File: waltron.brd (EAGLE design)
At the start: 45.4 x 47 mm, 21 parts, among them IC1 4049N, U1 LM386

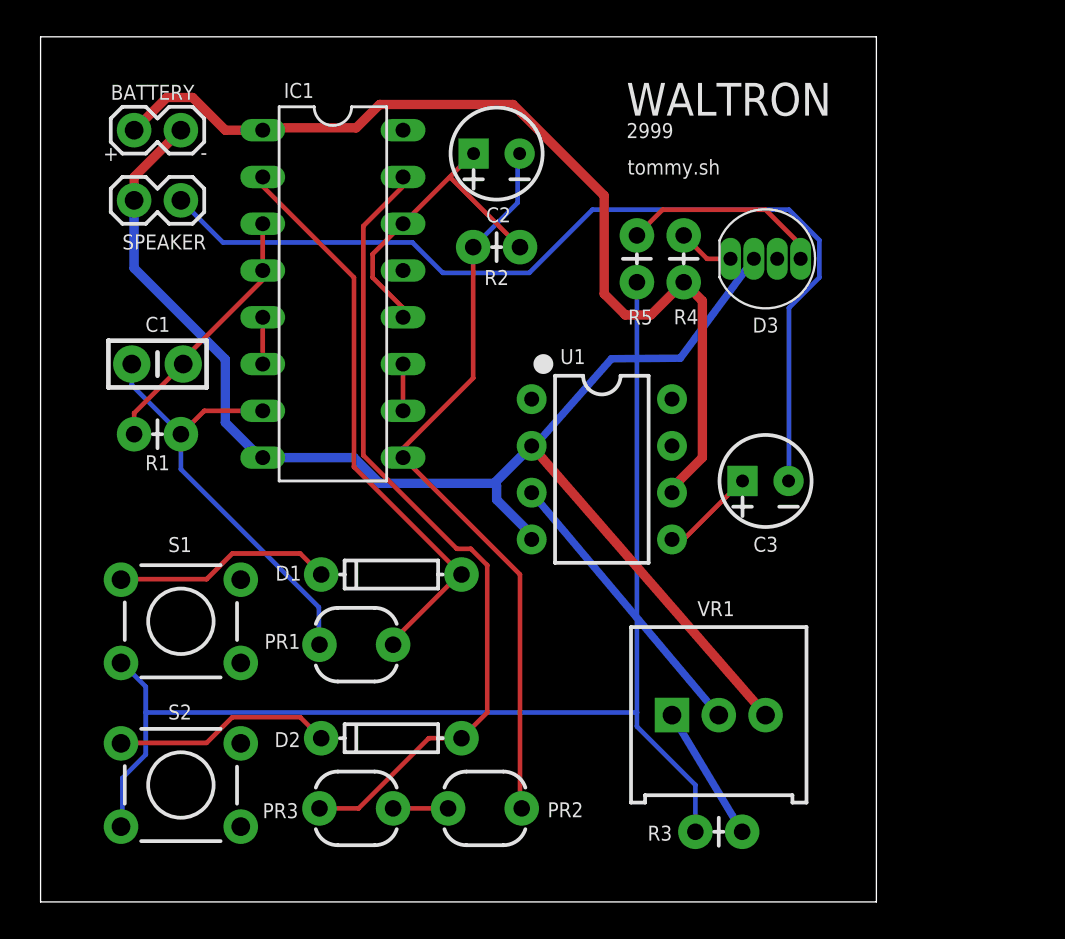
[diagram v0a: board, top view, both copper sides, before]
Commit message: Lay resistors flat, rip up routes
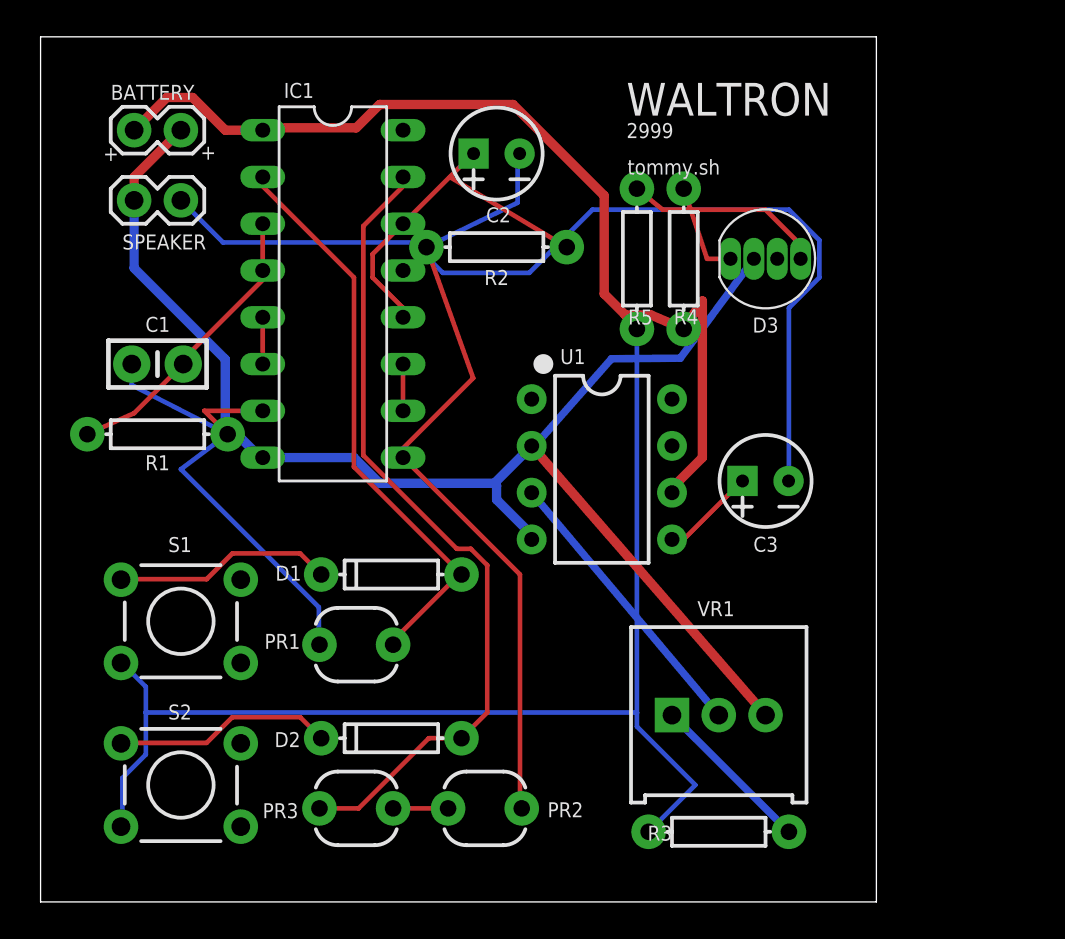
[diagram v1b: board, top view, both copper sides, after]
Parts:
- R1, R2, R4, R5: device SparkFun-Resistors:AXIAL-0.1 -> SparkFun-Resistors:AXIAL-0.3
- R3: value 10k -> 10K; device SparkFun-Resistors:AXIAL-0.1 -> SparkFun-Resistors:AXIAL-0.3
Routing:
- net N$3: track 24.5 -> 27.8 mm
- net N$5: track 41.0 -> 43.5 mm
- net N$18: track 3.07 -> 5.29 mm
- net N$7: track 17.2 -> 19.3 mm
- net N$2: track 14.3 -> 16.0 mm
- net N$13: track 7.39 -> 8.97 mm
- net N$12: track 67.9 -> 66.4 mm
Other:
- board text removed: "-"
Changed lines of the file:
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@@
 <text x="31.868003125" y="39.498728125" size="0.8128" layer="21" font="vector" ratio="10">tommy.sh</text>
 <text x="3.399725" y="40.238815625" size="0.8128" layer="21" font="vector" ratio="10">+</text>
-<text x="8.684678125" y="40.3093" size="0.8128" layer="21" font="vector" ratio="10">-</text>
+<text x="8.684678125" y="40.3093" size="0.8128" layer="21" font="vector" ratio="10">+</text>
 </plain>
 <attributes>
@@
 <attribute name="VALUE" x="17.145" y="11.811" size="0.6096" layer="27" font="vector" ratio="20" align="top-center"/>
 </element>
-<element name="R1" library="SparkFun-Resistors" package="AXIAL-0.1" value="1M" x="6.35" y="25.4" smashed="yes" rot="R180">
-<attribute name="PROD_ID" value="RES-09329" x="6.35" y="25.4" size="1.778" layer="27" rot="R180" display="off"/>
+<element name="R1" library="SparkFun-Resistors" package="AXIAL-0.3" value="1M" x="6.35" y="25.4" smashed="yes" rot="R180">
+<attribute name="PROD_ID" value="RES-12182" x="6.35" y="25.4" size="1.778" layer="27" rot="R180" display="off"/>
 <attribute name="NAME" x="6.35" y="24.257" size="0.8128" layer="25" font="vector" ratio="10" rot="R180" align="bottom-center"/>
 </element>
-<element name="R2" library="SparkFun-Resistors" package="AXIAL-0.1" value="1M" x="24.765" y="35.56" smashed="yes">
-<attribute name="PROD_ID" value="RES-09329" x="24.765" y="35.56" size="1.778" layer="27" display="off"/>
+<element name="R2" library="SparkFun-Resistors" package="AXIAL-0.3" value="1M" x="24.765" y="35.56" smashed="yes">
+<attribute name="PROD_ID" value="RES-12182" x="24.765" y="35.56" size="1.778" layer="27" display="off"/>
 <attribute name="NAME" x="24.765" y="33.502146875" size="0.8128" layer="25" font="vector" ratio="10" align="bottom-center"/>
 </element>
@@
 <attribute name="NAME" x="39.37" y="31.7329875" size="0.8128" layer="25" font="vector" ratio="10" rot="R180" align="bottom-center"/>
 </element>
-<element name="R5" library="SparkFun-Resistors" package="AXIAL-0.1" value="220" x="32.385" y="34.925" smashed="yes" rot="R90">
-<attribute name="PROD_ID" value="RES-09329" x="32.385" y="34.925" size="1.778" layer="27" rot="R90" display="off"/>
+<element name="R5" library="SparkFun-Resistors" package="AXIAL-0.3" value="220" x="32.385" y="34.925" smashed="yes" rot="R90">
+<attribute name="PROD_ID" value="RES-12182" x="32.385" y="34.925" size="1.778" layer="27" rot="R90" display="off"/>
 <attribute name="NAME" x="32.572125" y="32.170478125" size="0.8128" layer="25" font="vector" ratio="10" rot="R180" align="bottom-center"/>
 </element>
-<element name="R4" library="SparkFun-Resistors" package="AXIAL-0.1" value="220" x="34.925" y="34.925" smashed="yes" rot="R90">
-<attribute name="PROD_ID" value="RES-09329" x="34.925" y="34.925" size="1.778" layer="27" rot="R90" display="off"/>
+<element name="R4" library="SparkFun-Resistors" package="AXIAL-0.3" value="220" x="34.925" y="34.925" smashed="yes" rot="R90">
+<attribute name="PROD_ID" value="RES-12182" x="34.925" y="34.925" size="1.778" layer="27" rot="R90" display="off"/>
 <attribute name="NAME" x="35.052653125" y="32.1799125" size="0.8128" layer="25" font="vector" ratio="10" rot="R180" align="bottom-center"/>
 </element>
-<element name="R3" library="SparkFun-Resistors" package="AXIAL-0.1" value="10k" x="36.83" y="3.81" smashed="yes">
-<attribute name="PROD_ID" value="RES-09329" x="36.83" y="3.81" size="1.778" layer="27" display="off"/>
+<element name="R3" library="SparkFun-Resistors" package="AXIAL-0.3" value="10K" x="36.83" y="3.81" smashed="yes">
+<attribute name="PROD_ID" value="RES-12182" x="36.83" y="3.81" size="1.778" layer="27" display="off"/>
 <attribute name="NAME" x="33.6312875" y="3.328028125" size="0.8128" layer="25" font="vector" ratio="10" align="bottom-center"/>
 </element>
@@
 <wire x1="7.747" y1="29.464" x2="12.065" y2="33.782" width="0.254" layer="1"/>
 <wire x1="7.747" y1="29.21" x2="7.747" y2="29.464" width="0.254" layer="1"/>
-<wire x1="5.08" y1="26.543" x2="5.08" y2="25.4" width="0.254" layer="1"/>
+<wire x1="5.08" y1="26.543" x2="2.54" y2="25.4" width="0.254" layer="1"/>
 <wire x1="7.747" y1="29.21" x2="5.08" y2="26.543" width="0.254" layer="1"/>
 </signal>
@@
 <contactref element="C1" pad="1"/>
 <wire x1="8.89" y1="26.67" x2="12.065" y2="26.67" width="0.254" layer="1"/>
-<wire x1="7.62" y1="25.4" x2="8.89" y2="26.67" width="0.254" layer="1"/>
+<wire x1="10.16" y1="25.4" x2="8.89" y2="26.67" width="0.254" layer="1"/>
 <wire x1="15.113" y1="16.002" x2="15.113" y2="13.97" width="0.254" layer="16"/>
 <wire x1="7.62" y1="23.495" x2="15.113" y2="16.002" width="0.254" layer="16"/>
-<wire x1="7.62" y1="25.4" x2="7.62" y2="23.495" width="0.254" layer="16"/>
+<wire x1="10.16" y1="25.4" x2="7.62" y2="23.495" width="0.254" layer="16"/>
 <wire x1="15.113" y1="13.97" x2="15.145" y2="13.97" width="0.254" layer="16"/>
 <wire x1="4.953" y1="28.067" x2="4.953" y2="29.21" width="0.254" layer="16"/>
-<wire x1="7.62" y1="25.4" x2="4.953" y2="28.067" width="0.254" layer="16"/>
+<wire x1="10.16" y1="25.4" x2="4.953" y2="28.067" width="0.254" layer="16"/>
 </signal>
 <signal name="N$4">
@@
 <wire x1="19.685" y1="24.638" x2="19.685" y2="24.13" width="0.254" layer="1"/>
 <wire x1="23.495" y1="28.448" x2="19.685" y2="24.638" width="0.254" layer="1"/>
-<wire x1="23.495" y1="35.56" x2="23.495" y2="28.448" width="0.254" layer="1"/>
+<wire x1="20.955" y1="35.56" x2="23.495" y2="28.448" width="0.254" layer="1"/>
 <wire x1="25.908" y1="37.973" x2="25.908" y2="40.64" width="0.254" layer="16"/>
-<wire x1="23.495" y1="35.56" x2="25.908" y2="37.973" width="0.254" layer="16"/>
+<wire x1="20.955" y1="35.56" x2="25.908" y2="37.973" width="0.254" layer="16"/>
 <wire x1="25.908" y1="40.64" x2="26.015" y2="40.64" width="0.254" layer="16"/>
 <wire x1="26.035" y1="17.78" x2="26.035" y2="5.08" width="0.254" layer="1"/>
@@
 <wire x1="22.225" y1="39.37" x2="23.495" y2="40.64" width="0.254" layer="1"/>
 <wire x1="23.495" y1="40.64" x2="23.515" y2="40.64" width="0.254" layer="1"/>
-<wire x1="22.225" y1="39.37" x2="26.035" y2="35.56" width="0.254" layer="1"/>
+<wire x1="22.225" y1="39.37" x2="28.575" y2="35.56" width="0.254" layer="1"/>
 </signal>
 <signal name="N$8">
@@
 <wire x1="4.445" y1="4.191" x2="4.3688" y2="4.0894" width="0.254" layer="16"/>
 <wire x1="4.445" y1="12.954" x2="4.3688" y2="12.9794" width="0.254" layer="16"/>
-<wire x1="35.56" y1="6.35" x2="35.56" y2="3.81" width="0.254" layer="16"/>
+<wire x1="35.56" y1="6.35" x2="33.02" y2="3.81" width="0.254" layer="16"/>
 <wire x1="32.385" y1="9.525" x2="35.56" y2="6.35" width="0.254" layer="16"/>
-<wire x1="32.385" y1="33.655" x2="32.385" y2="10.287" width="0.254" layer="16"/>
+<wire x1="32.385" y1="31.115" x2="32.385" y2="10.287" width="0.254" layer="16"/>
 <wire x1="32.385" y1="10.287" x2="32.385" y2="9.525" width="0.254" layer="16"/>
 <wire x1="32.385" y1="10.287" x2="5.715" y2="10.287" width="0.254" layer="16"/>
@@
 <wire x1="39.37" y1="37.592" x2="41.275" y2="35.687" width="0.254" layer="1"/>
 <wire x1="33.782" y1="37.592" x2="39.37" y2="37.592" width="0.254" layer="1"/>
-<wire x1="32.385" y1="36.195" x2="33.782" y2="37.592" width="0.254" layer="1"/>
+<wire x1="32.385" y1="38.735" x2="33.782" y2="37.592" width="0.254" layer="1"/>
 </signal>
 <signal name="N$18">
@@
 <contactref element="D3" pad="1"/>
 <wire x1="36.195" y1="34.925" x2="37.465" y2="34.925" width="0.254" layer="1"/>
-<wire x1="34.925" y1="36.195" x2="36.195" y2="34.925" width="0.254" layer="1"/>
+<wire x1="34.925" y1="38.735" x2="36.195" y2="34.925" width="0.254" layer="1"/>
 </signal>
 <signal name="V+" class="1">
@@
 <wire x1="35.941" y1="24.13" x2="34.29" y2="22.479" width="0.508" layer="1"/>
 <wire x1="35.941" y1="32.639" x2="35.941" y2="24.13" width="0.508" layer="1"/>
-<wire x1="34.925" y1="33.655" x2="35.941" y2="32.639" width="0.508" layer="1"/>
+<wire x1="34.925" y1="31.115" x2="35.941" y2="32.639" width="0.508" layer="1"/>
 <wire x1="17.145" y1="42.037" x2="12.192" y2="42.037" width="0.508" layer="1"/>
 <wire x1="18.415" y1="43.307" x2="17.145" y2="42.037" width="0.508" layer="1"/>
@@
 <wire x1="31.75" y1="31.877" x2="30.607" y2="33.02" width="0.508" layer="1"/>
 <wire x1="33.147" y1="31.877" x2="31.75" y2="31.877" width="0.508" layer="1"/>
-<wire x1="34.925" y1="33.655" x2="33.147" y2="31.877" width="0.508" layer="1"/>
+<wire x1="34.925" y1="31.115" x2="33.147" y2="31.877" width="0.508" layer="1"/>
 <wire x1="12.192" y1="42.037" x2="12.065" y2="41.91" width="0.508" layer="1"/>
 </signal>
@@
 <contactref element="R3" pad="P$2"/>
 <contactref element="VR1" pad="1"/>
-<wire x1="34.29" y1="10.145" x2="38.1" y2="3.81" width="0.4064" layer="16"/>
+<wire x1="34.29" y1="10.145" x2="40.64" y2="3.81" width="0.4064" layer="16"/>
 </signal>
 <signal name="N$16">

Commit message: Switch out trimmer
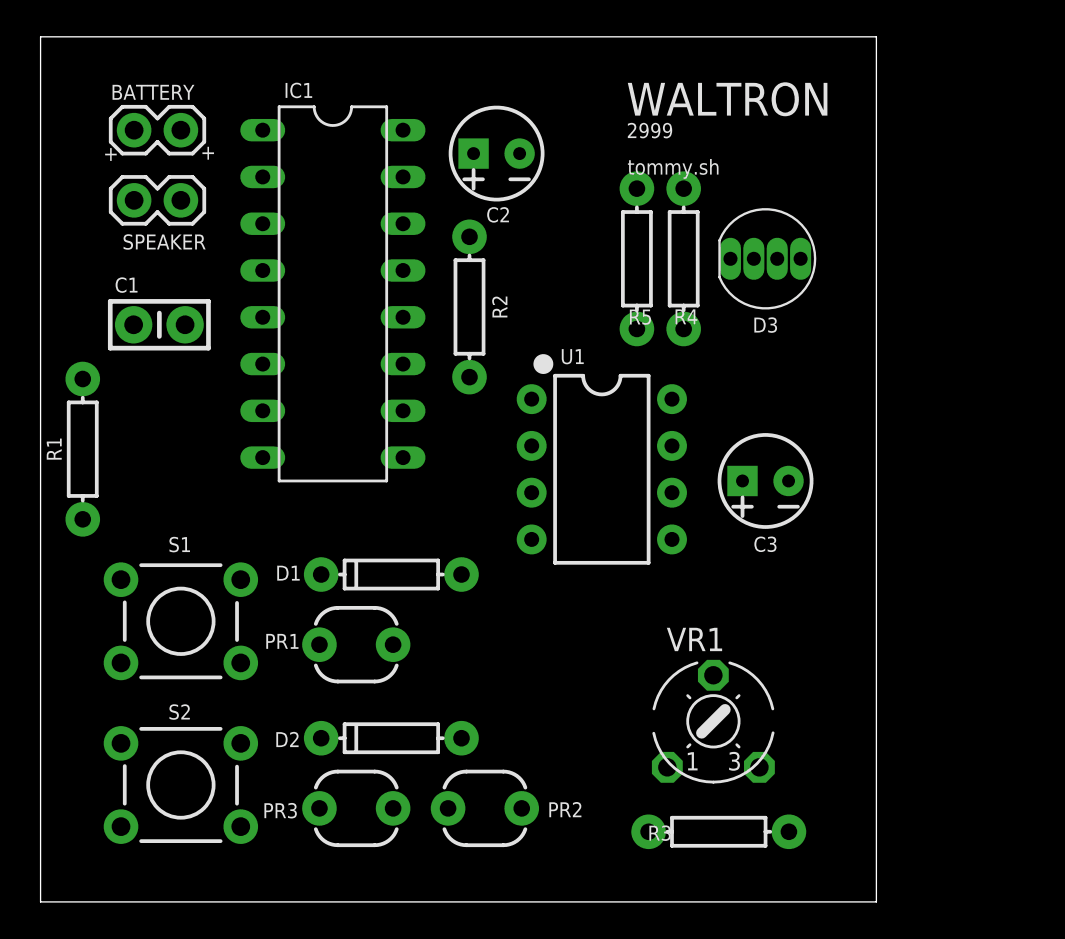
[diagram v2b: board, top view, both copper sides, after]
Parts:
- VR1: value 5k -> 5K; device SparkFun-Resistors:TRIMPOT-PTH-3386U -> adafruit:6MM
- moved R1 4.14 mm to (2.29, 24.6), turned to 90 degrees
- moved R2 3.57 mm to (23.3, 32.3), turned to 90 degrees
- moved C1 2.14 mm to (6.45, 31.3)
- moved VR1 0.46 mm to (36.5, 9.81)
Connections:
- net GND: now also VR1.A; no longer VR1.3
- net N$13: now also VR1.E; no longer VR1.1
- net N$16: now also VR1.S; no longer VR1.2
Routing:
- net GND: track 78.1 -> 0.00 mm
- net N$12: track 66.4 -> 0.00 mm
- net V+: track 52.8 -> 0.00 mm
- net N$15: track 52.2 -> 0.00 mm
- net N$8: track 44.5 -> 0.00 mm
- net N$5: track 43.5 -> 0.00 mm
- net N$4: track 31.5 -> 0.00 mm
- net N$3: track 27.8 -> 0.00 mm
- net N$7: track 19.3 -> 0.00 mm
- net N$2: track 16.0 -> 0.00 mm
- net N$16: track 15.8 -> 0.00 mm
- net N$11: track 11.9 -> 0.00 mm
- net N$9: track 11.9 -> 0.00 mm
- net N$17: track 10.8 -> 0.00 mm
- net N$13: track 8.97 -> 0.00 mm
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
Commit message: Rearrange components, iterate version to 2999.1
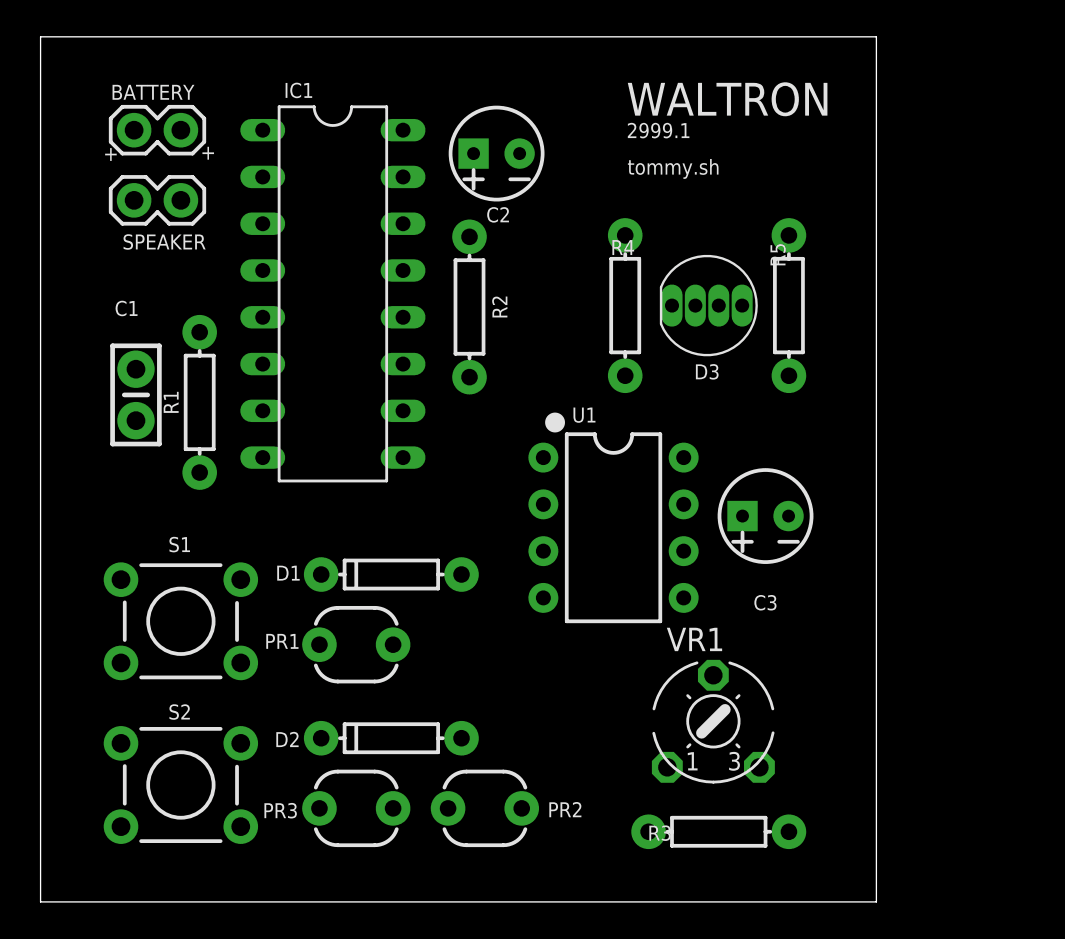
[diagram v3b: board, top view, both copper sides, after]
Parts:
- moved R5 8.64 mm to (40.6, 32.4), turned to 270 degrees
- moved R1 6.84 mm to (8.64, 27.1)
- moved D3 4.07 mm to (36.2, 32.4)
- moved R4 4.07 mm to (31.8, 32.4), turned to 270 degrees
- moved C1 4.02 mm to (5.18, 27.5), turned to 90 degrees
- moved U1 3.24 mm to (31.1, 20.3)
- moved C3 1.91 mm to (39.4, 21.0)
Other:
- board text added: "2999.1"
- board text removed: "2999"

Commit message: More rearrangement, separating out optional on-board parts
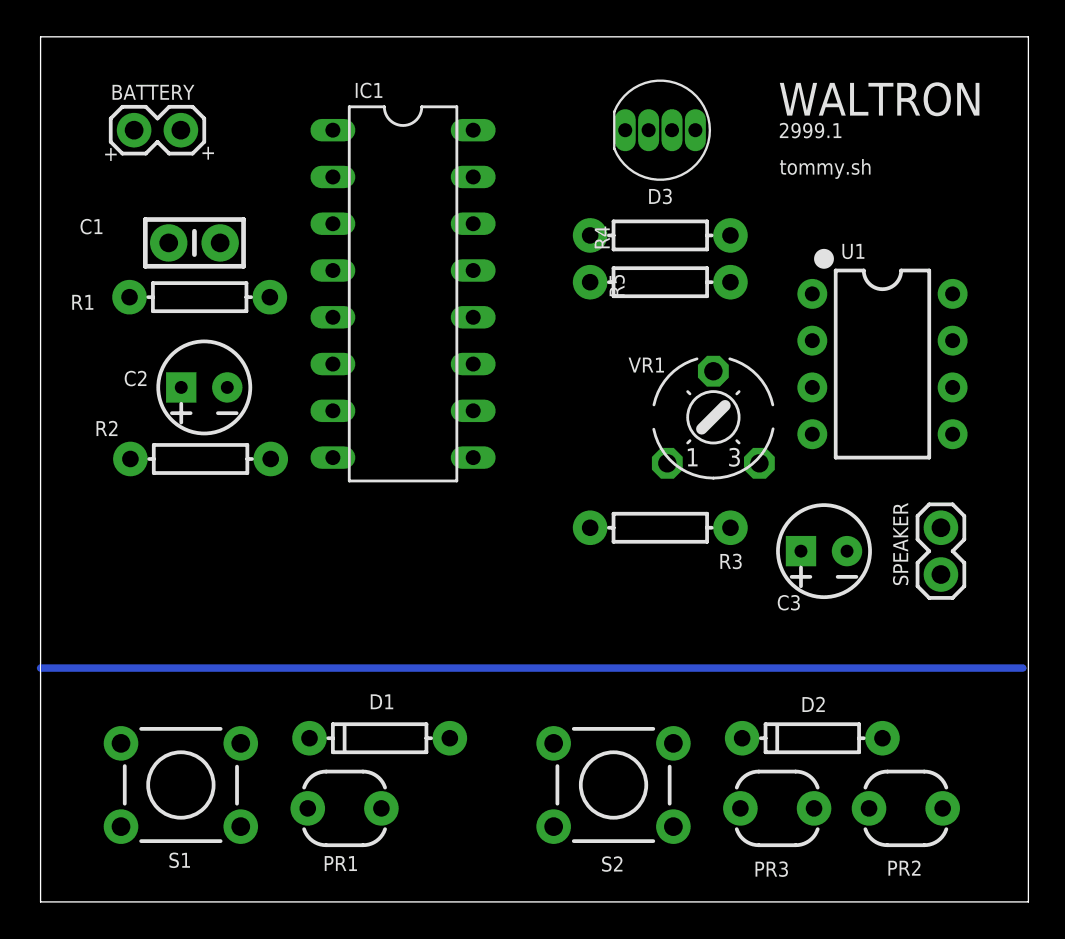
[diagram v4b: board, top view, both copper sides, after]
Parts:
- moved SPEAKER 44.9 mm to (48.9, 20.3), turned to 270 degrees
- moved S2 23.5 mm to (31.1, 6.35)
- moved PR2 22.9 mm to (47.0, 5.08)
- moved PR3 22.9 mm to (40.0, 5.08)
- moved D2 22.9 mm to (41.9, 8.89)
- moved C2 20.3 mm to (8.89, 27.9)
- moved U1 17.1 mm to (45.7, 29.2)
- moved R3 16.8 mm to (33.7, 20.3), turned to 180 degrees
- moved R2 16.8 mm to (8.69, 24.1), turned to 180 degrees
- moved VR1 16.5 mm to (36.5, 26.3)
- moved D3 9.86 mm to (33.7, 41.9)
- moved D1 8.91 mm to (18.4, 8.89)
- moved PR1 8.91 mm to (16.5, 5.08)
- moved S1 8.89 mm to (7.62, 6.35)
- moved C1 8.84 mm to (8.36, 35.8), turned to 0 degrees
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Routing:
- net N$19: track 0.00 -> 53.3 mm
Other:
- board size 45.4 x 47 mm -> 53.6 x 47 mm
